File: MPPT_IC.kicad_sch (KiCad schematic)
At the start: 1 part

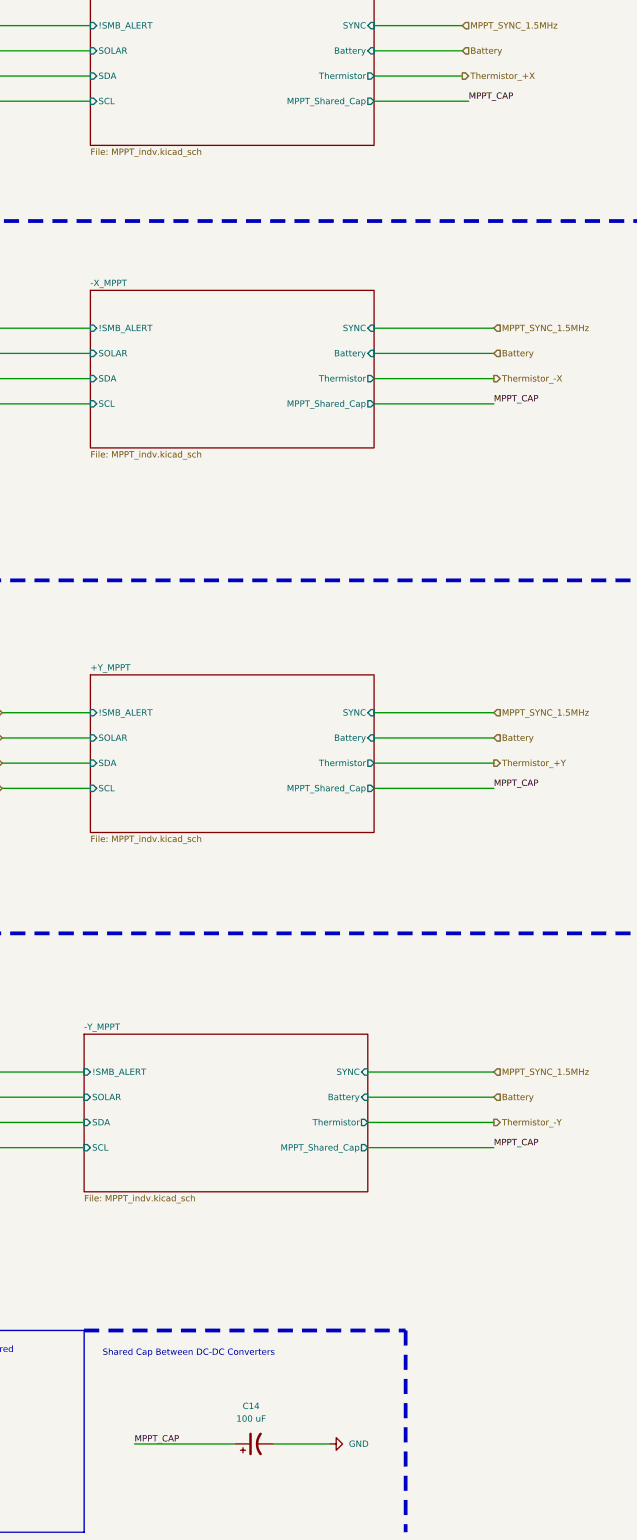
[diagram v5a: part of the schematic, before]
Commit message: Changed LTC 4412 to 4417, still kinks to work out
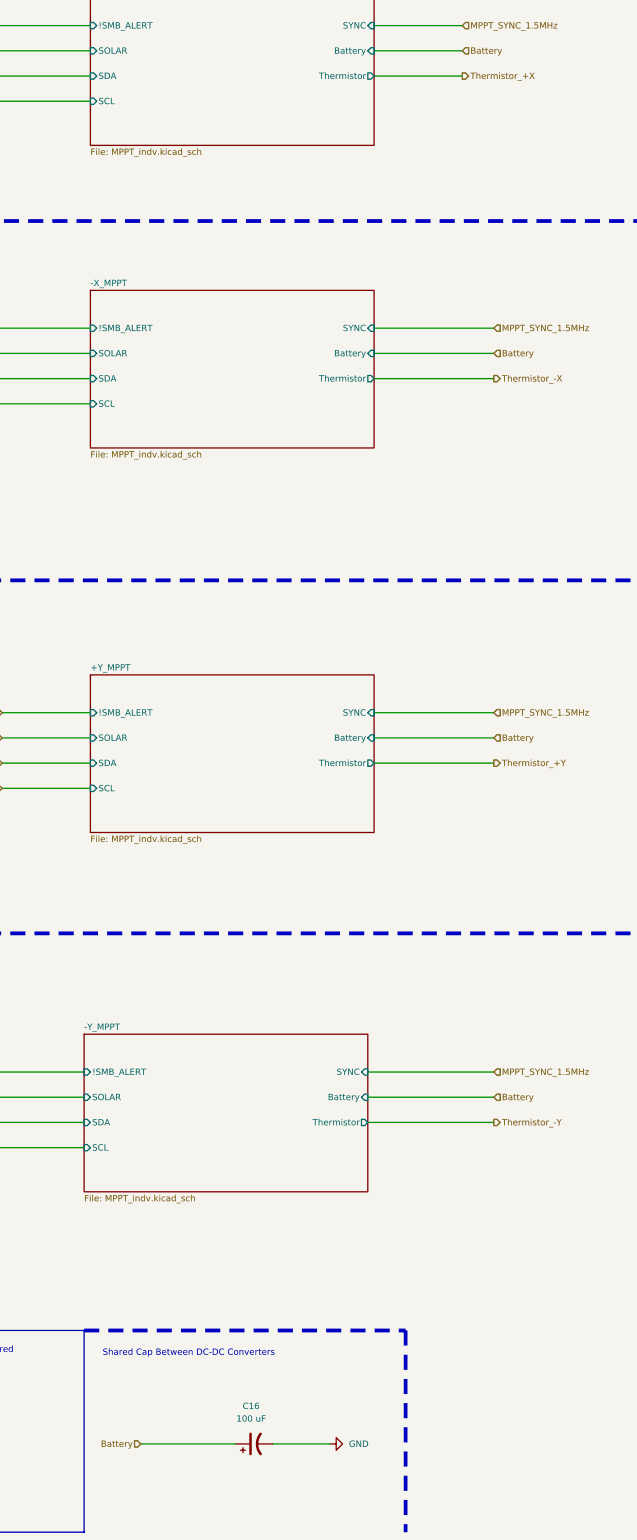
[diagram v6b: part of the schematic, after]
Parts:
- renumbered C14 to C16
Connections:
- net MPPT_CAP is gone; now on net Battery: C16.1
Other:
- sheet +X_MPPT ports: added none; removed MPPT_Shared_Cap
- sheet +Y_MPPT ports: added none; removed MPPT_Shared_Cap
- sheet -X_MPPT ports: added none; removed MPPT_Shared_Cap
- sheet -Y_MPPT ports: added none; removed MPPT_Shared_Cap
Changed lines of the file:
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@@
-	(wire
-		(pts
-			(xy 194.31 186.69) (xy 170.18 186.69)
-		)
-		(stroke
-			(width 0)
-			(type default)
-		)
-	)
-	(wire
-		(pts
-			(xy 170.18 109.22) (xy 194.31 109.22)
-		)
-		(stroke
-			(width 0)
-			(type default)
-		)
-	)
 	(wire
 		(pts
@@
 	(wire
 		(pts
-			(xy 121.92 318.77) (xy 142.24 318.77)
+			(xy 123.19 318.77) (xy 142.24 318.77)
 		)
 		(stroke
@@
 	(wire
 		(pts
-			(xy 194.31 259.08) (xy 168.91 259.08)
-		)
-		(stroke
-			(width 0)
-			(type default)
-		)
-	)
-	(wire
-		(pts
 			(xy 95.25 181.61) (xy 113.03 181.61)
 		)
@@
 		(pts
 			(xy 93.98 104.14) (xy 113.03 104.14)
-		)
-		(stroke
-			(width 0)
-			(type default)
-		)
-	)
-	(wire
-		(pts
-			(xy 170.18 48.26) (xy 189.23 48.26)
 		)
 		(stroke
@@
 			(width 0)
 			(type default)
-		)
-	)
-	(label "MPPT_CAP"
-		(at 194.31 109.22 0)
-		(effects
-			(font
-				(size 1.27 1.27)
-			)
-			(justify left bottom)
-		)
-	)
-	(label "MPPT_CAP"
-		(at 189.23 48.26 0)
-		(effects
-			(font
-				(size 1.27 1.27)
-			)
-			(justify left bottom)
-		)
-	)
-	(label "MPPT_CAP"
-		(at 194.31 259.08 0)
-		(effects
-			(font
-				(size 1.27 1.27)
-			)
-			(justify left bottom)
-		)
-	)
-	(label "MPPT_CAP"
-		(at 121.92 318.77 0)
-		(effects
-			(font
-				(size 1.27 1.27)
-			)
-			(justify left bottom)
-		)
-	)
-	(label "MPPT_CAP"
-		(at 194.31 186.69 0)
-		(effects
-			(font
-				(size 1.27 1.27)
-			)
-			(justify left bottom)
 		)
 	)
@@
 			)
 			(justify left)
+		)
+	)
+	(hierarchical_label "Battery"
+		(shape input)
+		(at 123.19 318.77 180)
+		(effects
+			(font
+				(size 1.27 1.27)
+			)
+			(justify right)
 		)
 	)
@@
 		(dnp no)
 		(fields_autoplaced yes)
-		(property "Reference" "C14"
+		(property "Reference" "C16"
 			(at 145.415 311.15 90)
 			(effects
@@
 			(project "EPS_mppt_board"
 				(path "/8f246f89-1ec7-4136-9977-839b50e116ed/cba64b11-23b0-44e2-88c6-aa38d0b150b4"
-					(reference "C14")
+					(reference "C16")
 					(unit 1)
 				)
@@
 		(dnp no)
 		(fields_autoplaced yes)
-		(property "Reference" "#PWR030"
+		(property "Reference" "#PWR035"
 			(at 167.64 318.77 0)
 			(effects
@@
 			(project "EPS_mppt_board"
 				(path "/8f246f89-1ec7-4136-9977-839b50e116ed/cba64b11-23b0-44e2-88c6-aa38d0b150b4"
-					(reference "#PWR030")
+					(reference "#PWR035")
 					(unit 1)
 				)
@@
 			)
 		)
-		(pin "MPPT_Shared_Cap" output
-			(at 170.18 109.22 0)
-			(effects
-				(font
-					(size 1.27 1.27)
-				)
-				(justify right)
-			)
-		)
 		(pin "SYNC" input
 			(at 170.18 93.98 0)
@@
 			)
 		)
-		(pin "MPPT_Shared_Cap" output
-			(at 170.18 186.69 0)
-			(effects
-				(font
-					(size 1.27 1.27)
-				)
-				(justify right)
-			)
-		)
 		(pin "SYNC" input
 			(at 170.18 171.45 0)
@@
 			)
 		)
-		(pin "MPPT_Shared_Cap" output
-			(at 170.18 48.26 0)
-			(effects
-				(font
-					(size 1.27 1.27)
-				)
-				(justify right)
-			)
-		)
 		(pin "SYNC" input
 			(at 170.18 33.02 0)
@@
 			)
 		)
-		(pin "MPPT_Shared_Cap" output
-			(at 168.91 259.08 0)
-			(effects
-				(font
-					(size 1.27 1.27)
-				)
-				(justify right)
-			)
-		)

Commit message: small changes
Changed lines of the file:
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@@
 	(text "Shared Cap Between DC-DC Converters"
 		(exclude_from_sim no)
-		(at 132.842 300.482 0)
+		(at 135.89 299.212 0)
 		(effects
 			(font
-				(size 1.27 1.27)
+				(size 1.524 1.524)
 			)
 		)

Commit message: Started PCB layout
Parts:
- removed C16: 100 uF, Capacitor_Tantalum_SMD:CP_EIA-7361-38_AVX-V, symbol Device:C_Polarized_US
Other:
- sheet +X_MPPT ports: added OUTPUT; removed Battery
- sheet +Y_MPPT ports: added OUTPUT; removed Battery
- sheet -X_MPPT ports: added OUTPUT; removed Battery
- sheet -Y_MPPT ports: added OUTPUT; removed Battery
- note removed: "Shared Cap Between DC-DC Converters"
